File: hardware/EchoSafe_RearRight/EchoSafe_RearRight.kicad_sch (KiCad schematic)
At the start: 4 parts, among them J1 Conn_Harness_07, M3 C0720B001F

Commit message: Assign footprints across all 5 projects, add missing fp-lib-table
Target confirmed as a compact near-final wearable, not an early bring-up
prototype -- choices below favor small/soldered over socketed/header.

Fixed a regression: splitting into 5 projects had wiped the mic
(LGA_CAV_IVS) and motor (C0720B001F:XDCR_C0720B001F) footprints that
already existed pre-split -- the instance generator zeroed every new
component's footprint unconditionally. Restored both from the pre-split
commit.

Fixed a second, pre-existing bug: no fp-lib-table ever existed in any
version of this project (same class of gap as the sym-lib-table issue
found earlier this session), and three footprint references
(LGA_CAV_IVS, ESP32-S3-WROOM-1_EXP, 21-0136I_T1633-4_MXM) were bare
names with no library prefix -- neither would have resolved in KiCad's
PCB editor even with a table present. Created fp-lib-table in the
central pod (ESP32-S3-WROOM-1, MAX98357AETE-T) and all 4 module projects
(ICS-43434, C0720B001F), then added the missing prefixes. Verified every
path resolves to a real .kicad_mod file on disk.

Newly assigned:
- All 17 capacitors -> Capacitor_SMD:C_0603_1608Metric
- BT1 (battery) -> Connector_JST:JST_PH_S2B_PH_K_1x02_P2.00mm_Horizontal
  (confirmed: this battery ships with a pre-attached JST-PH connector)
- LD1 (LD1117V33) -> 3-pin 2.54mm header pattern (matches the real
  breakout's hole spacing regardless of pins-vs-wire assembly)
- J1/central pod (TP4056) -> 4-pin 2.54mm header pattern (placeholder --
  flagged to verify against the actual purchased board's hole spacing)
- J2-J5 (pod) + each module's J1 -> JST-SH 1.0mm pitch, 9-pin or 7-pin
  (compact-wearable target ruled out bulkier 2.54mm headers for a
  7-9-conductor cable through the headband)

Left unassigned: LS1/LS2 (speakers) -- no specific part chosen yet,
capsule dimensions vary too much to guess a meaningful footprint.

Verified across all 5 files independently: paren balance intact, no
duplicate UUIDs, no duplicate re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
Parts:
- C11: footprint (none) -> Capacitor_SMD:C_0603_1608Metric
- J1: footprint (none) -> Connector_JST:JST_SH_BM07B-SRSS-TB_1x07-1MP_P1.00mm_Horizontal
- M3: footprint (none) -> C0720B001F:XDCR_C0720B001F
- MIC3: footprint (none) -> ICS-43434:LGA_CAV_IVS
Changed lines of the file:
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@@
 			(effects (font (size 1.27 1.27)) (justify left))
 		)
-		(property "Footprint" ""
+		(property "Footprint" "ICS-43434:LGA_CAV_IVS"
 			(at 50 50 0)
 			(effects (font (size 1.27 1.27) (italic yes)) (hide yes))
@@
 			(effects (font (size 1.27 1.27)) (justify left))
 		)
-		(property "Footprint" ""
+		(property "Footprint" "Capacitor_SMD:C_0603_1608Metric"
 			(at 30 50 0)
 			(effects (font (size 1.27 1.27) (italic yes)) (hide yes))
@@
 			(effects (font (size 1.27 1.27)) (justify left))
 		)
-		(property "Footprint" ""
+		(property "Footprint" "C0720B001F:XDCR_C0720B001F"
 			(at 50 90 0)
 			(effects (font (size 1.27 1.27) (italic yes)) (hide yes))
@@
 			(effects (font (size 1.27 1.27)) (justify left))
 		)
-		(property "Footprint" ""
+		(property "Footprint" "Connector_JST:JST_SH_BM07B-SRSS-TB_1x07-1MP_P1.00mm_Horizontal"
 			(at 120 50 0)
 			(effects (font (size 1.27 1.27) (italic yes)) (hide yes))

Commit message: Fix JST-SH footprint naming error, verify TP4056 pin spacing
Resolved both gaps flagged at the end of the footprint pass:

- JST-SH harness connector names were an unverified guess using a
  "BM0xB-SRSS-TB" prefix. Fetched the actual files from KiCad's own
  kicad-footprints repo and confirmed the real prefix is "SM0xB-SRSS-TB"
  -- JST_SH_SM09B-SRSS-TB_1x09-1MP_P1.00mm_Horizontal (9 signal + 2
  mounting pads) and JST_SH_SM07B-SRSS-TB_1x07-1MP_P1.00mm_Horizontal
  (7 signal + 2 mounting pads) both verified to exist with correct pad
  counts. Fixed all 8 occurrences across all 5 projects (J2/J3/J4/J5 in
  the central pod, one J1 per module).

- Checked TP4056 module pin spacing against multiple independent
  sources; 2.54mm/0.1" through-hole pitch is standard across common
  module variants, confirming the PinHeader_1x04_P2.54mm_Vertical
  placeholder already assigned. Noted this should still get a quick
  physical check against the actual board, since "HiLetGo TP4056"
  covers slightly different revisions.

Verified across all 5 files: paren balance intact, unique UUIDs.

Co-Authored-By: Claude Sonnet 5 <noreply@anthropic.com>
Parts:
- J1: footprint Connector_JST:JST_SH_BM07B-SRSS-TB_1x07-1MP_P1.00mm_Horizontal -> Connector_JST:JST_SH_SM07B-SRSS-TB_1x07-1MP_P1.00mm_Horizontal
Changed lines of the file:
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@@
 			(effects (font (size 1.27 1.27)) (justify left))
 		)
-		(property "Footprint" "Connector_JST:JST_SH_BM07B-SRSS-TB_1x07-1MP_P1.00mm_Horizontal"
+		(property "Footprint" "Connector_JST:JST_SH_SM07B-SRSS-TB_1x07-1MP_P1.00mm_Horizontal"
 			(at 120 50 0)
 			(effects (font (size 1.27 1.27) (italic yes)) (hide yes))

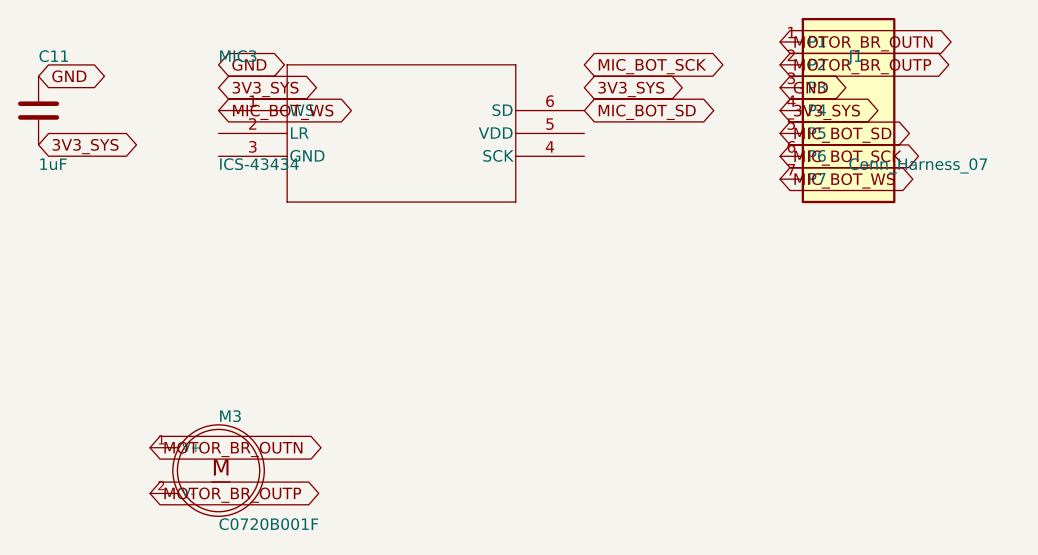
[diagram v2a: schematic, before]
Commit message: Fix session-wide Y-axis coordinate bug, power the ESP32 module
Discovered KiCad is actually installed on this machine and ran real
kicad-cli sch erc against every schematic for the first time, instead of
continuing to rely on text-based invariant checks alone. This surfaced a
fundamental bug affecting every schematic edit made this session:

Every label/wire/no-connect placed with a nonzero local Y pin offset used
placement_y + local_y instead of the correct placement_y - local_y --
KiCad symbol graphics are authored Y-up, the sheet is Y-down, and that
flip applies even at angle=0/no-mirror. The two formulas only agree when
local_y=0, which is why isolated spot-checks earlier in the session
happened to look right.

Fixed via a from-scratch single-pass correction (not sequential in-place
edits -- an earlier attempt at that approach introduced a second bug,
caught before committing: correcting one label could make its new
position collide with a not-yet-corrected label's old position, causing
a later step to move the wrong element). Final approach computes every
correction from an unmodified snapshot and applies them all in one pass
from a fixed baseline.

Verified by ERC before/after, not by the tooling that produced the bug:
- All 4 module projects: 21/21/17/17 raw violations -> 9/9/8/8, all
  expected (spare GPIOs, the already-documented placeholder-connector
  warning, and cross-project "power not driven" since the driving
  component lives in a different project's file).
- Central pod: down to 0 dangling labels, 0 genuinely unconnected pins.
  Remaining ~200 ERC items are exclusively pairwise power-rail type-
  mismatch warnings (expected on any board with this many ICs sharing
  3V3_SYS/GND), cosmetic off-grid warnings, and spare pins.

Also fixed, a genuine gap this same ERC pass surfaced (unrelated to the
Y-axis bug): the ESP32 module's own 3V3/GND/EN pins were never wired to
anything -- every peripheral got connected this session, the MCU's own
supply pins we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
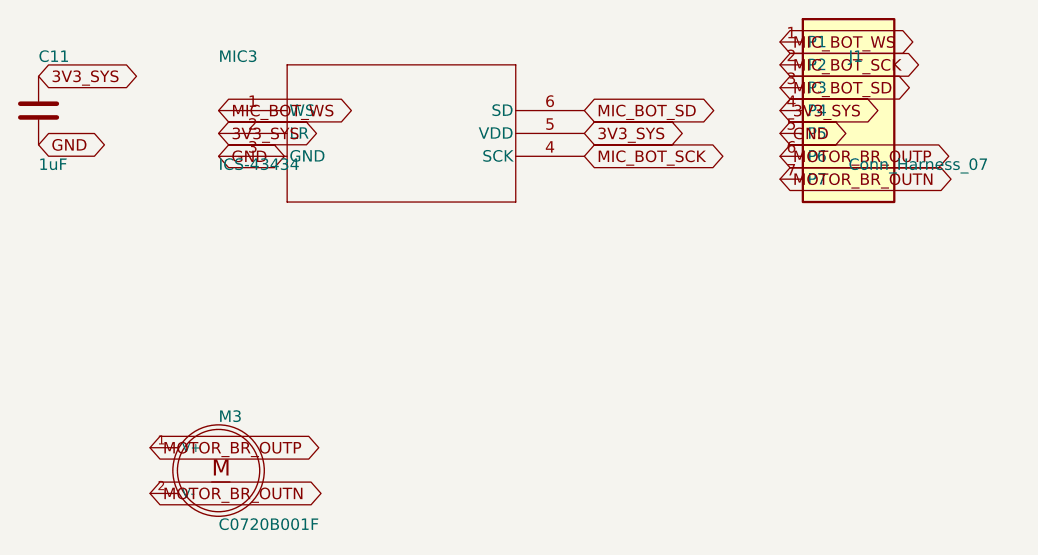
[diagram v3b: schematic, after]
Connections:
- net 3V3_SYS: now also C11.1, MIC3.2 (LR), MIC3.5 (VDD); no longer C11.2
- net GND: now also C11.2, J1.5 (P5), MIC3.3 (GND); no longer C11.1, J1.3 (P3)
- net MIC_BOT_SCK: now also J1.2 (P2), MIC3.4 (SCK); no longer J1.6 (P6)
- net MIC_BOT_SD: now also J1.3 (P3); no longer J1.5 (P5)
- net MIC_BOT_WS: now also J1.1 (P1); no longer J1.7 (P7)
- net MOTOR_BR_OUTN: now also J1.7 (P7), M3.2 (V-); no longer J1.1 (P1), M3.1 (V+)
- net MOTOR_BR_OUTP: now also J1.6 (P6), M3.1 (V+); no longer J1.2 (P2), M3.2 (V-)
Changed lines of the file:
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@@
 	(global_label "3V3_SYS"
 		(shape bidirectional)
-		(at 50 47.46 0)
-		(fields_autoplaced yes)
-		(effects
-			(font
-				(size 1.27 1.27)
-			)
-			(justify left)
-		)
-		(property "Intersheetrefs" "${INTERSHEET_REFS}"
-			(at 55 47.46 0)
+		(at 50 52.54 0)
+		(fields_autoplaced yes)
+		(effects
+			(font
+				(size 1.27 1.27)
+			)
+			(justify left)
+		)
+		(property "Intersheetrefs" "${INTERSHEET_REFS}"
+			(at 55 52.54 0)
 			(effects
 				(font
@@
 	(global_label "GND"
 		(shape bidirectional)
-		(at 50 44.92 0)
-		(fields_autoplaced yes)
-		(effects
-			(font
-				(size 1.27 1.27)
-			)
-			(justify left)
-		)
-		(property "Intersheetrefs" "${INTERSHEET_REFS}"
-			(at 55 44.92 0)
+		(at 50 55.08 0)
+		(fields_autoplaced yes)
+		(effects
+			(font
+				(size 1.27 1.27)
+			)
+			(justify left)
+		)
+		(property "Intersheetrefs" "${INTERSHEET_REFS}"
+			(at 55 55.08 0)
 			(effects
 				(font
@@
 	(global_label "MIC_BOT_SCK"
 		(shape bidirectional)
-		(at 90.64 44.92 0)
-		(fields_autoplaced yes)
-		(effects
-			(font
-				(size 1.27 1.27)
-			)
-			(justify left)
-		)
-		(property "Intersheetrefs" "${INTERSHEET_REFS}"
-			(at 95.64 44.92 0)
+		(at 90.64 55.08 0)
+		(fields_autoplaced yes)
+		(effects
+			(font
+				(size 1.27 1.27)
+			)
+			(justify left)
+		)
+		(property "Intersheetrefs" "${INTERSHEET_REFS}"
+			(at 95.64 55.08 0)
 			(effects
 				(font
@@
 	(global_label "3V3_SYS"
 		(shape bidirectional)
-		(at 90.64 47.46 0)
-		(fields_autoplaced yes)
-		(effects
-			(font
-				(size 1.27 1.27)
-			)
-			(justify left)
-		)
-		(property "Intersheetrefs" "${INTERSHEET_REFS}"
-			(at 95.64 47.46 0)
+		(at 90.64 52.54 0)
+		(fields_autoplaced yes)
+		(effects
+			(font
+				(size 1.27 1.27)
+			)
+			(justify left)
+		)
+		(property "Intersheetrefs" "${INTERSHEET_REFS}"
+			(at 95.64 52.54 0)
 			(effects
 				(font
@@
 	(global_label "3V3_SYS"
 		(shape bidirectional)
+		(at 30 46.19 0)
+		(fields_autoplaced yes)
+		(effects
+			(font
+				(size 1.27 1.27)
+			)
+			(justify left)
+		)
+		(property "Intersheetrefs" "${INTERSHEET_REFS}"
+			(at 35 46.19 0)
+			(effects
+				(font
+					(size 1.27 1.27)
+				)
+				(justify left)
+				(hide yes)
+			)
+		)
+	)
+	(global_label "GND"
+		(shape bidirectional)
 		(at 30 53.81 0)
 		(fields_autoplaced yes)
@@
 		(property "Intersheetrefs" "${INTERSHEET_REFS}"
 			(at 35 53.81 0)
-			(effects
-				(font
-					(size 1.27 1.27)
-				)
-				(justify left)
-				(hide yes)
-			)
-		)
-	)
-	(global_label "GND"
-		(shape bidirectional)
-		(at 30 46.19 0)
-		(fields_autoplaced yes)
-		(effects
-			(font
-				(size 1.27 1.27)
-			)
-			(justify left)
-		)
-		(property "Intersheetrefs" "${INTERSHEET_REFS}"
-			(at 35 46.19 0)
 			(effects
 				(font
@@
 	(global_label "MOTOR_BR_OUTP"
 		(shape bidirectional)
+		(at 42.38 87.46 0)
+		(fields_autoplaced yes)
+		(effects
+			(font
+				(size 1.27 1.27)
+			)
+			(justify left)
+		)
+		(property "Intersheetrefs" "${INTERSHEET_REFS}"
+			(at 47.38 87.46 0)
+			(effects
+				(font
+					(size 1.27 1.27)
+				)
+				(justify left)
+				(hide yes)
+			)
+		)
+	)
+	(global_label "MOTOR_BR_OUTN"
+		(shape bidirectional)
 		(at 42.38 92.54 0)
 		(fields_autoplaced yes)
@@
 		(property "Intersheetrefs" "${INTERSHEET_REFS}"
 			(at 47.38 92.54 0)
-			(effects
-				(font
-					(size 1.27 1.27)
-				)
-				(justify left)
-				(hide yes)
-			)
-		)
-	)
-	(global_label "MOTOR_BR_OUTN"
-		(shape bidirectional)
-		(at 42.38 87.46 0)
-		(fields_autoplaced yes)
-		(effects
-			(font
-				(size 1.27 1.27)
-			)
-			(justify left)
-		)
-		(property "Intersheetrefs" "${INTERSHEET_REFS}"
-			(at 47.38 87.46 0)
 			(effects
 				(font
@@
 	(global_label "MIC_BOT_WS"
 		(shape bidirectional)
+		(at 112.38 42.38 0)
+		(fields_autoplaced yes)
+		(effects
+			(font
+				(size 1.27 1.27)
+			)
+			(justify left)
+		)
+		(property "Intersheetrefs" "${INTERSHEET_REFS}"
+			(at 117.38 42.38 0)
+			(effects
+				(font
+					(size 1.27 1.27)
+				)
+				(justify left)
+				(hide yes)
+			)
+		)
+	)
+	(global_label "MIC_BOT_SCK"
+		(shape bidirectional)
+		(at 112.38 44.92 0)
+		(fields_autoplaced yes)
+		(effects
+			(font
+				(size 1.27 1.27)
+			)
+			(justify left)
+		)
+		(property "Intersheetrefs" "${INTERSHEET_REFS}"
+			(at 117.38 44.92 0)
+			(effects
+				(font
+					(size 1.27 1.27)
+				)
+				(justify left)
+				(hide yes)
+			)
+		)
+	)
+	(global_label "MIC_BOT_SD"
+		(shape bidirectional)
+		(at 112.38 47.46 0)
+		(fields_autoplaced yes)
+		(effects
+			(font
+				(size 1.27 1.27)
+			)
+			(justify left)
+		)
+		(property "Intersheetrefs" "${INTERSHEET_REFS}"
+			(at 117.38 47.46 0)
+			(effects
+				(font
+					(size 1.27 1.27)
+				)
+				(justify left)
+				(hide yes)
+			)
+		)
+	)
+	(global_label "3V3_SYS"
+		(shape bidirectional)
+		(at 112.38 50 0)
+		(fields_autoplaced yes)
+		(effects
+			(font
+				(size 1.27 1.27)
+			)
+			(justify left)
+		)
+		(property "Intersheetrefs" "${INTERSHEET_REFS}"
+			(at 117.38 50 0)
+			(effects
+				(font
+					(size 1.27 1.27)
+				)
+				(justify left)
+				(hide yes)
+			)
+		)
+	)
+	(global_label "GND"
+		(shape bidirectional)
+		(at 112.38 52.54 0)
+		(fields_autoplaced yes)
+		(effects
+			(font
+				(size 1.27 1.27)
+			)
+			(justify left)
+		)
+		(property "Intersheetrefs" "${INTERSHEET_REFS}"
+			(at 117.38 52.54 0)
+			(effects
+				(font
+					(size 1.27 1.27)
+				)
+				(justify left)
+				(hide yes)
+			)
+		)
+	)
+	(global_label "MOTOR_BR_OUTP"
+		(shape bidirectional)
+		(at 112.38 55.08 0)
+		(fields_autoplaced yes)
+		(effects
+			(font
+				(size 1.27 1.27)
+			)
+			(justify left)
+		)
+		(property "Intersheetrefs" "${INTERSHEET_REFS}"
+			(at 117.38 55.08 0)
+			(effects
+				(font
+					(size 1.27 1.27)
+				)
+				(justify left)
+				(hide yes)
+			)
+		)
+	)
+	(global_label "MOTOR_BR_OUTN"
+		(shape bidirectional)
 		(at 112.38 57.62 0)
 		(fields_autoplaced yes)
@@
 			(effects
 				(font
-					(size 1.27 1.27)
-				)
-				(justify left)
-				(hide yes)
-			)
-		)
-	)
-	(global_label "MIC_BOT_SCK"
-		(shape bidirectional)
-		(at 112.38 55.08 0)
-		(fields_autoplaced yes)
-		(effects
-			(font
-				(size 1.27 1.27)
-			)
-			(justify left)
-		)
-		(property "Intersheetrefs" "${INTERSHEET_REFS}"
-			(at 117.38 55.08 0)
-			(effects
-				(font
-					(size 1.27 1.27)
-				)
-				(justify left)
-				(hide yes)
-			)
-		)
-	)
-	(global_label "MIC_BOT_SD"
-		(shape bidirectional)
-		(at 112.38 52.54 0)
-		(fields_autoplaced yes)
-		(effects
-			(font
-				(size 1.27 1.27)
-			)
-			(justify left)
-		)
-		(property "Intersheetrefs" "${INTERSHEET_REFS}"
-			(at 117.38 52.54 0)
-			(effects
-				(font
-					(size 1.27 1.27)
-				)
-				(justify left)
-				(hide yes)
-			)
-		)
-	)
-	(global_label "3V3_SYS"
-		(shape bidirectional)
-		(at 112.38 50 0)
-		(fields_autoplaced yes)
-		(effects
-			(font
-				(size 1.27 1.27)
-			)
-			(justify left)
-		)
-		(property "Intersheetrefs" "${INTERSHEET_REFS}"
-			(at 117.38 50 0)
-			(effects
-				(font
-					(size 1.27 1.27)
-				)
-				(justify left)
-				(hide yes)
-			)
-		)
-	)
-	(global_label "GND"
-		(shape bidirectional)
-		(at 112.38 47.46 0)
-		(fields_autoplaced yes)
-		(effects
-			(font
-				(size 1.27 1.27)
-			)
-			(justify left)
-		)
-		(property "Intersheetrefs" "${INTERSHEET_REFS}"
-			(at 117.38 47.46 0)
-			(effects
-				(font
-					(size 1.27 1.27)
-				)
-				(justify left)
-				(hide yes)
-			)
-		)
-	)
-	(global_label "MOTOR_BR_OUTP"
-		(shape bidirectional)
-		(at 112.38 44.92 0)
-		(fields_autoplaced yes)
-		(effects
-			(font
-				(size 1.27 1.27)
-			)
-			(justify left)
-		)
-		(property "Intersheetrefs" "${INTERSHEET_REFS}"
-			(at 117.38 44.92 0)
-			(effects
-				(font
-					(size 1.27 1.27)
-				)
-				(justify left)
-				(hide yes)
-			)
-		)
-	)
-	(global_label "MOTOR_BR_OUTN"
-		(shape bidirectional)
-		(at 112.38 42.38 0)
-		(fields_autoplaced yes)
-		(effects
-			(font
-				(size 1.27 1.27)
-			)
-			(justify left)
-		)
-		(property "Intersheetrefs" "${INTERSHEET_REFS}"
-			(at 117.38 42.38 0)
-			(effects
-				(font

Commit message: Replace mic footprint with one authored from the real datasheet
Discovered while starting PCB placement: the original SnapEDA-imported
LGA_CAV_IVS.kicad_mod (pre-dates this session) doesn't match the real
ICS-43434 part. Its GND pad (3) is a tiny 0.127x0.127mm corner pad, and
a non-electrical mechanical hole occupies pad number "6", pushing the
real 6th electrical pad to "7" -- one off from the schematic symbol's
pin 6 (SD).

Fetched and read InvenSense's actual datasheet (DS-000069 Rev 1.0) to
verify: GND is really a large ring pad (1.025mm inner / 1.625mm outer
diameter) surrounding the microphone's acoustic port -- nothing like
what the footprint had.

Authored a replacement footprint (ICS-43434_LGA6, new library
Mics_Corrected.pretty) using KiCad's own pcbnew Python API directly from
the datasheet's Figure 3 (pin positions) and Figure 13 (land pattern
dimensions): 5 roundrect signal pads at the datasheet's stated 0.6x0.9mm
size / 0.9mm pitch, GND simplified to a solid circular pad at the ring's
outer diameter (electrically equivalent, though it omits the board-level
acoustic port hole the datasheet also specifies -- that's a PCB-outline
feature, not something a footprint file can express, and is flagged in
CLAUDE.md as a manual step for actual layout).

Round-trip verified by reloading the saved file through
pcbnew.FootprintLoad() and checking pad count/positions/shapes. Updated
fp-lib-table in all 4 module projects and MIC1-4's Footprint property.
Re-ran ERC afterward -- unchanged (9/9/8/8), confirming this was purely
a physical/PCB-level fix with no schematic-connectivity impact.

Co-Authored-By: Claude Sonnet 5 <noreply@anthropic.com>
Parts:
- MIC3: footprint ICS-43434:LGA_CAV_IVS -> ICS-43434:ICS-43434_LGA6
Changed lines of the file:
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@@
 			(effects (font (size 1.27 1.27)) (justify left))
 		)
-		(property "Footprint" "ICS-43434:LGA_CAV_IVS"
+		(property "Footprint" "ICS-43434:ICS-43434_LGA6"
 			(at 50 50 0)
 			(effects (font (size 1.27 1.27) (italic yes)) (hide yes))

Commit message: Generate fab outputs (gerbers, drill, CPL, BOM) for all 5 boards
kicad-cli pcb export gerbers/drill/pos and sch export bom, into each
project's own outputs/ folder, zipped for direct fab upload. Standard
2-layer gerber set (confirmed 2-layer by checking the layer table, not
assumed); drill files split PTH/NPTH since the mic modules have a real
NPTH hole (H1, the acoustic port) -- spot-checked the NPTH file directly
to confirm it's really in there.

Generating the BOM surfaced a real gap: J2/J3/J4/J5 (central pod), J1
(all 4 modules), and LS1 (front modules) still had their schematic
Footprint field pointing at the stock Connector_JST/Connector_Molex
footprint, not the Connectors_PinMarked override from the last commit --
because that fix only touched footprint instances already placed on the
PCB, never the originating schematic symbols. Left alone, a future
"Update PCB from Schematic" would have silently reverted the pin-marker
fix. Fixed by updating the Footprint property in each .kicad_sch;
confirmed via kicad-cli sch erc that violation counts on all 5 schematics
are unchanged (metadata-only edit, no electrical effect).

All 5 boards reconfirmed at 0 DRC violations, full severity.

Co-Authored-By: Claude Sonnet 5 <noreply@anthropic.com>
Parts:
- J1: footprint Connector_JST:JST_SH_SM07B-SRSS-TB_1x07-1MP_P1.00mm_Horizontal -> Connectors_PinMarked:JST_SH_SM07B-SRSS-TB_1x07-1MP_P1.00mm_Horizontal
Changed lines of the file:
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@@
 			(effects (font (size 1.27 1.27)) (justify left))
 		)
-		(property "Footprint" "Connector_JST:JST_SH_SM07B-SRSS-TB_1x07-1MP_P1.00mm_Horizontal"
+		(property "Footprint" "Connectors_PinMarked:JST_SH_SM07B-SRSS-TB_1x07-1MP_P1.00mm_Horizontal"
 			(at 120 50 0)
 			(effects (font (size 1.27 1.27) (italic yes)) (hide yes))
